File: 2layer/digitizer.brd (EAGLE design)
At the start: 76.2 x 51.3 mm, 56 parts, among them IC1 FT601QQFN76, X1 SMA-142-0711-881/886, X2 SMA-142-0711-881/886

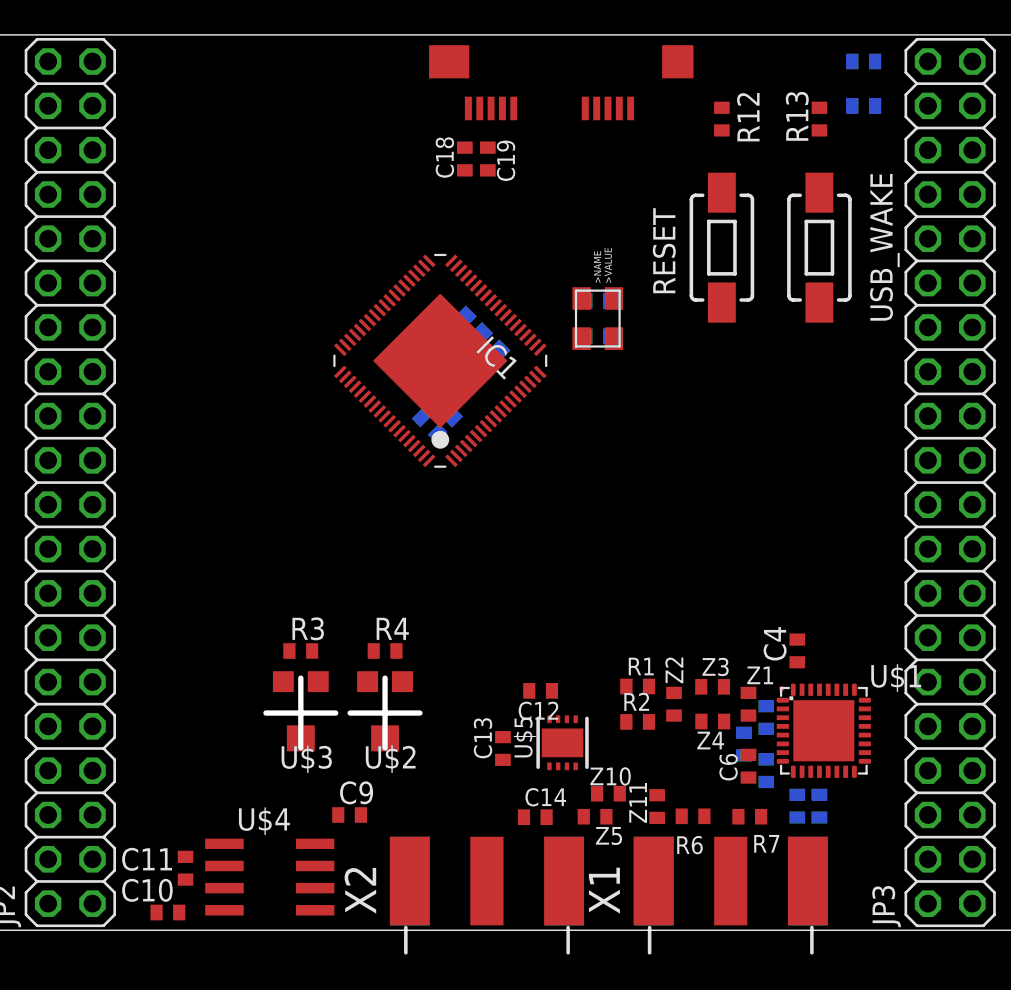
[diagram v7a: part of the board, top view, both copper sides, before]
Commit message: added dual regulator solution for power isolation
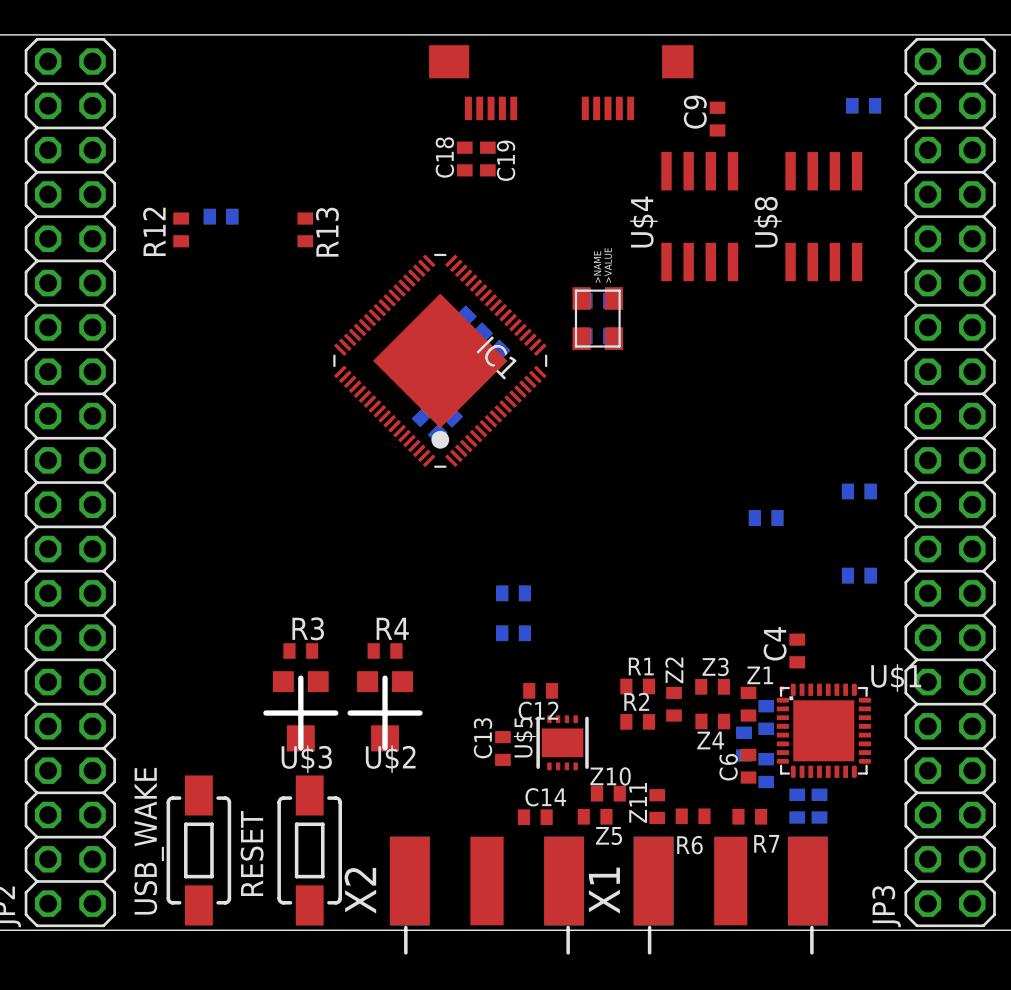
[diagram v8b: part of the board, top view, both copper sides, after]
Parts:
- added C23: 1u, resistor:C0402
- added C24: 0.01u, resistor:C0402
- added C25: 10u, resistor:C0402
- added U$8: LT1763CS8-3, linear-technology:SOIC8
- moved USB_WAKE 49.6 mm to (20.3, 4.57)
- moved U$4 45.2 mm to (49.0, 40.9), turned to 0 degrees
- moved C9 45.1 mm to (50.0, 46.5), turned to 90 degrees
- moved RESET 41.8 mm to (26.7, 4.57)
- moved R17 37.9 mm to (21.6, 40.9)
- moved R12 31.6 mm to (19.3, 40.1), turned to 90 degrees
- moved R13 30.1 mm to (26.4, 40.1), turned to 90 degrees
- moved C10 25.5 mm to (38.4, 17.0), flipped to the bottom, turned to 180 degrees
- moved C11 24.5 mm to (38.4, 19.3), flipped to the bottom, turned to 180 degrees
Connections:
- new net N$16: C24.2, U$8.4
- net AVDD: now also C24.1, C25.1, U$8.1, U$8.2; no longer C9.1, U$4.5, U$4.8
- net GND: now also C23.2, C25.2, U$8.3, U$8.6, U$8.7
- net VBUS: now also C23.1, C9.1, U$4.5, U$4.8, U$8.5, U$8.8
